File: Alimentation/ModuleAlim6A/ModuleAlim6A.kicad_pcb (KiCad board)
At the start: 4 copper layers, 66.5 x 39.8 mm, 19 parts, among them J1 Conn_01x05, J2 Conn_01x02, J3 OUTPUT, U1 PTN78020W_EUK-7, U2 ACS712xLCTR-20A

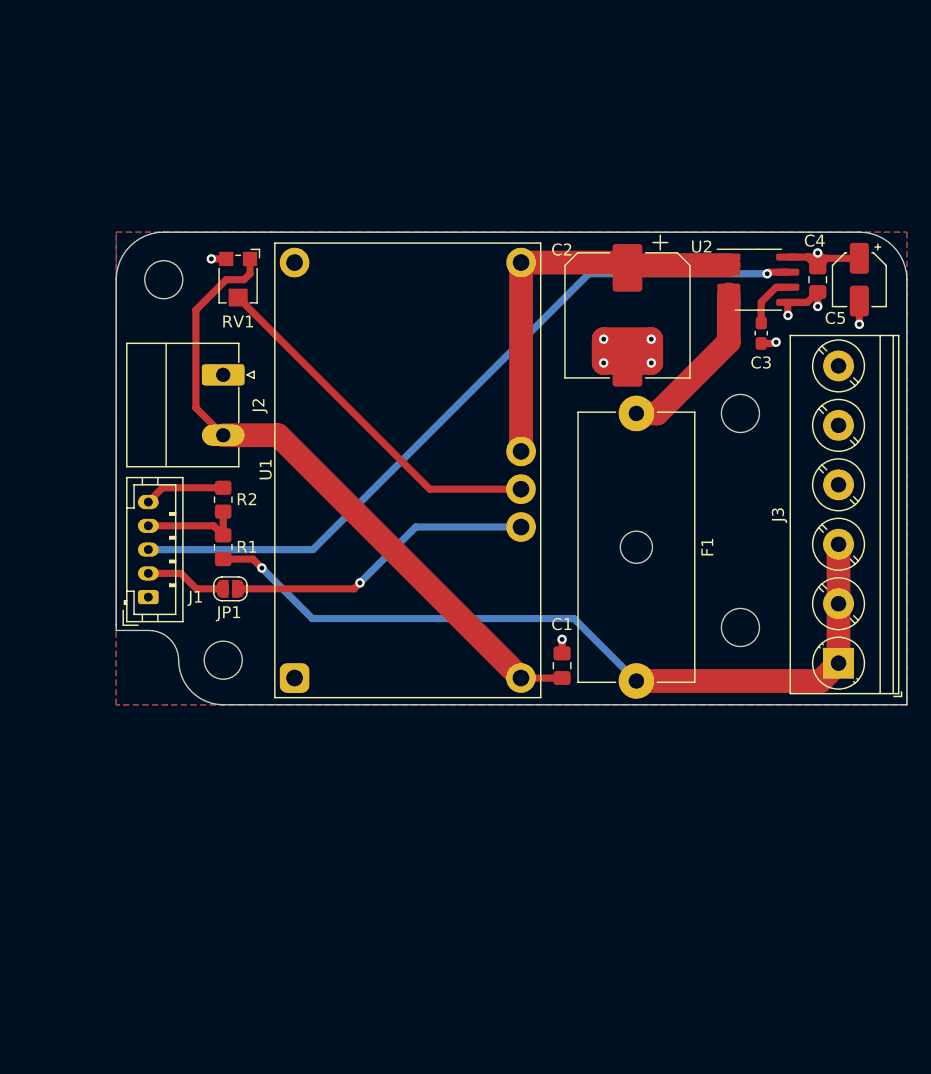
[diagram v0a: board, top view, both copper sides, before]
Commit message: Module alim ISO, clean master alim
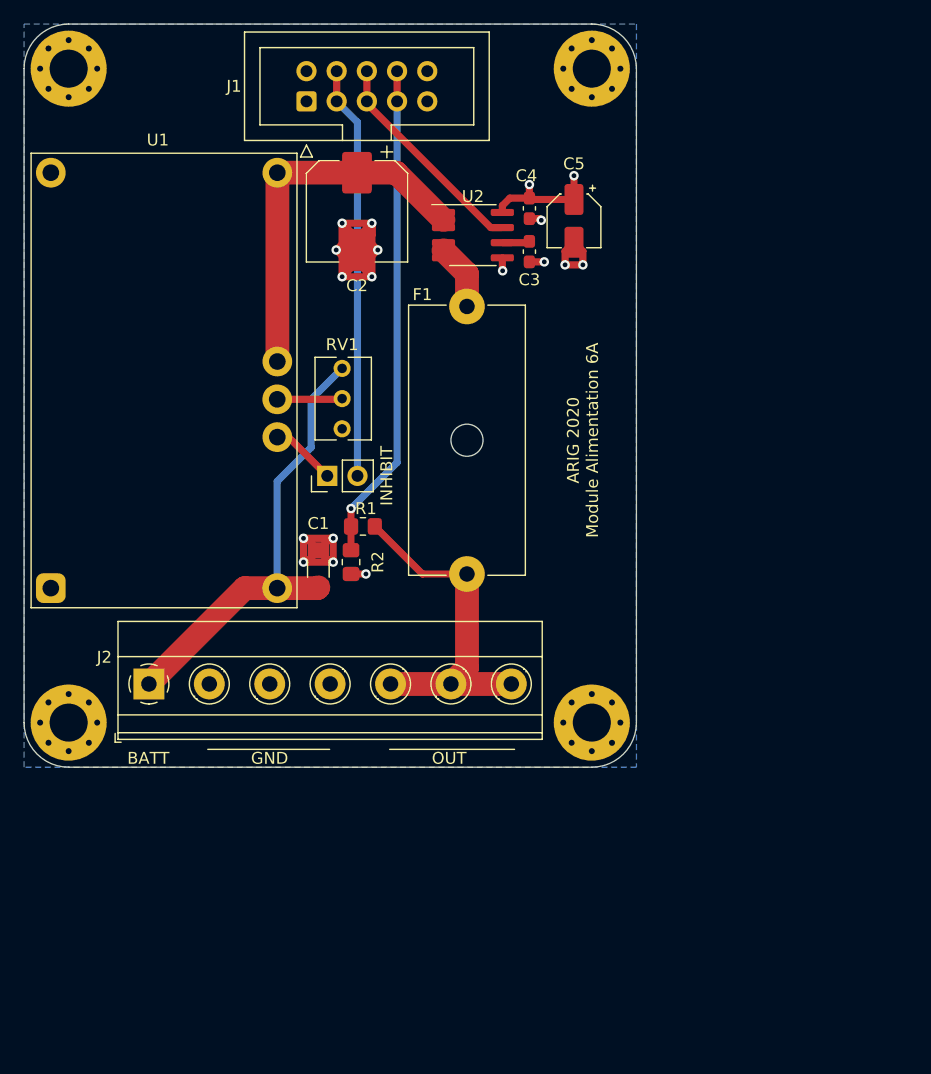
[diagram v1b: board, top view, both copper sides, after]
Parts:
- removed J3: OUTPUT, TerminalBlock_Phoenix:TerminalBlock_Phoenix_PT-1,5-6-5.0-H_1x06_P5.00mm_Horizontal
- removed JP1: /INHIBIT, Jumper:SolderJumper-2_P1.3mm_Open_RoundedPad1.0x1.5mm
- added J4: INHIBIT, Connector_PinHeader_2.54mm:PinHeader_1x02_P2.54mm_Vertical, F.Cu at (142.2, 85.5)
- C1: footprint Capacitor_SMD:C_0805_2012Metric_Pad1.18x1.45mm_HandSolder -> Capacitor_SMD:C_1206_3216Metric_Pad1.33x1.80mm_HandSolder
- C2: footprint Capacitor_SMD:CP_Elec_10x10 -> Capacitor_SMD:CP_Elec_8x10
- C4: footprint Capacitor_SMD:C_0805_2012Metric_Pad1.18x1.45mm_HandSolder -> Capacitor_SMD:C_0603_1608Metric_Pad1.08x0.95mm_HandSolder
- H1, H2, H3, H4: value MountingHole -> MountingHole_Pad; footprint MountingHole:MountingHole_3.2mm_M3 -> MountingHole:MountingHole_3.2mm_M3_Pad_Via
- J1: value Conn_01x05 -> Cmd; footprint Connector_JST:JST_PH_B5B-PH-K_1x05_P2.00mm_Vertical -> Connector_IDC:IDC-Header_2x05_P2.54mm_Vertical
- J2: value Conn_01x02 -> POWER; footprint Connector_Phoenix_MC_HighVoltage:PhoenixContact_MC_1,5_2-G-5.08_1x02_P5.08mm_Horizontal -> TerminalBlock_Phoenix:TerminalBlock_Phoenix_MKDS-1,5-7-5.08_1x07_P5.08mm_Horizontal
- RV1: footprint Potentiometer_SMD:Potentiometer_Bourns_TC33X_Vertical -> Potentiometer_THT:Potentiometer_Bourns_3266Y_Vertical
- moved H2 62.2 mm to (120.5, 106.2)
- moved H1 48.6 mm to (164.5, 51.2)
- moved J1 43.8 mm to (140.5, 54.0)
- moved H4 31.4 mm to (164.5, 106.2)
- moved J2 26.7 mm to (127.2, 103.0), turned to 0 degrees
- moved C4 25.0 mm to (159.2, 63.0)
- moved C5 24.5 mm to (163.0, 64.0)
- moved C2 24.4 mm to (144.8, 63.2)
- moved U2 24.3 mm to (154.5, 65.2)
- moved C1 22.1 mm to (141.5, 93.3)
- moved U1 21.8 mm to (119.0, 94.9)
- moved C3 20.7 mm to (159.2, 66.6)
- moved H3 19.5 mm to (120.5, 51.2)
- moved F1 16.9 mm to (154.0, 71.2)
- moved R2 12.0 mm to (144.2, 92.8), turned to 270 degrees
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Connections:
- H1 pad 1: (no net) -> GND
- H2 pad 1: (no net) -> GND
- H3 pad 1: (no net) -> GND
- H4 pad 1: (no net) -> GND
- J1 pad 2: /EN -> +5V
- J1 pad 3: /ANA_CURRENT -> /EN
- J1 pad 4: /ANA_VOLT -> /EN
- J1 pad 5: GND -> /ANA_CURRENT
- J2 pad 1: GND -> +BATT
- J2 pad 2: +BATT -> GND
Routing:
- net /ANA_CURRENT: track 63.4 -> 18.4 mm, vias 1 -> 0
- net /OUT: track 66.6 -> 29.4 mm, vias 1 -> 0
- net /ANA_VOLT: track 8.63 -> 41.9 mm, vias 0 -> 1
- net /EN: track 6.79 -> 34.8 mm
- net GND: track 29.7 -> 56.4 mm, vias 10 -> 16
- net Net-(RV1-Pad2): track 30.5 -> 5.48 mm
- net Net-(J4-Pad1): track 26.0 -> 5.55 mm, vias 1 -> 0
- net +BATT: track 55.5 -> 38.4 mm
- net Net-(F1-Pad1): track 15.5 -> 6.81 mm
- net Net-(C3-Pad1): track 4.50 -> 2.32 mm
- net /VO: track 34.9 -> 32.8 mm
- net +5V: vias 1 -> 2
- removed copper zone on F.Cu, net GND
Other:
- board size 66.5 x 39.8 mm -> 51.5 x 62.5 mm
- board text added: "ARIG 2020 Module Alimentation 6A"
- board text added: "BATT"
- board text added: "GND"
- board text added: "OUT"

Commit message: Modules Alim 3A et 6A uniforme sans mesure courant/tension
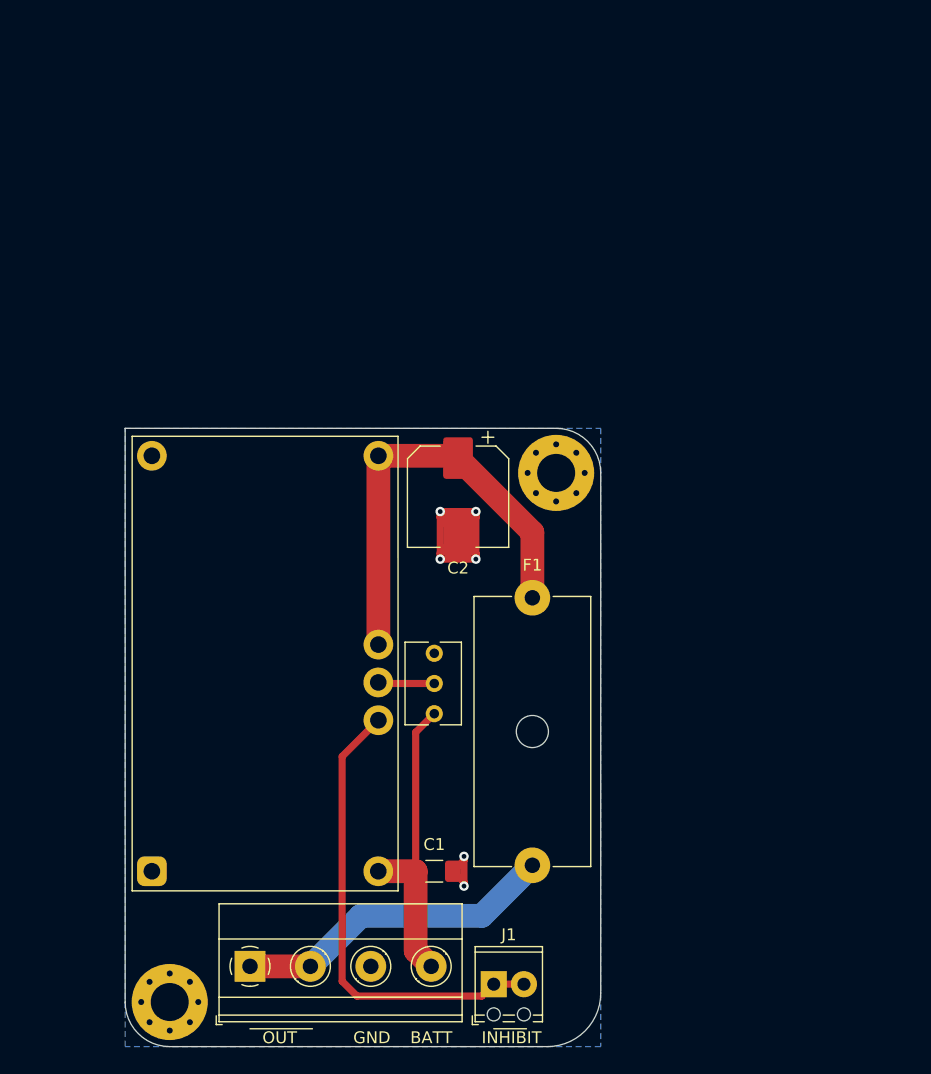
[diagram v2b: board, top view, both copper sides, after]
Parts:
- removed C3: 1n, Capacitor_SMD:C_0603_1608Metric_Pad1.08x0.95mm_HandSolder
- removed C4: 100n, Capacitor_SMD:C_0603_1608Metric_Pad1.08x0.95mm_HandSolder
- removed C5: 1u, Capacitor_SMD:CP_Elec_4x5.3
- removed H3, H4: MountingHole_Pad, MountingHole:MountingHole_3.2mm_M3_Pad_Via
- removed J4: INHIBIT, Connector_PinHeader_2.54mm:PinHeader_1x02_P2.54mm_Vertical
- removed R1: 10K, Resistor_SMD:R_0805_2012Metric_Pad1.20x1.40mm_HandSolder
- removed R2: 6.2K, Resistor_SMD:R_0805_2012Metric_Pad1.20x1.40mm_HandSolder
- removed U2: ACS712xLCTR-20A, Package_SO:SOIC-8_3.9x4.9mm_P1.27mm
- J1: value Cmd -> Inhibit; footprint Connector_IDC:IDC-Header_2x05_P2.54mm_Vertical -> TerminalBlock_Phoenix:TerminalBlock_Phoenix_MPT-0,5-2-2.54_1x02_P2.54mm_Horizontal
- J2: value POWER -> Alim. IN / OUT; footprint TerminalBlock_Phoenix:TerminalBlock_Phoenix_MKDS-1,5-7-5.08_1x07_P5.08mm_Horizontal -> TerminalBlock_Phoenix:TerminalBlock_Phoenix_MKDS-1,5-4-5.08_1x04_P5.08mm_Horizontal
- moved H1 86.2 mm to (129.0, 129.8)
- moved J1 75.9 mm to (156.2, 128.2), turned to 0 degrees
- moved F1 47.3 mm to (159.5, 118.2), turned to 90 degrees
- moved H2 46.1 mm to (161.5, 85.2)
- moved RV1 30.1 mm to (151.2, 105.5), turned to 270 degrees
- moved C1 27.2 mm to (151.2, 118.8), turned to 0 degrees
- moved C2 25.5 mm to (153.2, 87.2)
- moved U1 25.3 mm to (127.5, 118.8)
- moved J2 25.2 mm to (135.8, 126.8)
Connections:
- C2 pad 1: /VO -> Net-(C2-Pad1)
- F1 pad 1: Net-(F1-Pad1) -> /OUT
- F1 pad 2: /OUT -> Net-(C2-Pad1)
- J1 pad 1: +5V -> /EN
- J1 pad 2: +5V -> /EN
- J2 pad 1: +BATT -> /OUT
- J2 pad 2: GND -> /OUT
- J2 pad 4: GND -> +BATT
- U1 pad 3: Net-(J4-Pad1) -> /EN
- U1 pad 5: /VO -> Net-(C2-Pad1)
- U1 pad 6: /VO -> Net-(C2-Pad1)
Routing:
- net /ANA_VOLT: track 41.9 -> 0.00 mm, vias 1 -> 0
- net Net-(C2-Pad1): track 0.00 -> 37.0 mm
- net /VO: track 32.8 -> 0.00 mm
- net GND: track 56.4 -> 30.3 mm, vias 16 -> 6
- net /ANA_CURRENT: track 18.4 -> 0.00 mm
- net +BATT: track 38.4 -> 25.6 mm
- net +5V: track 10.0 -> 0.00 mm, vias 2 -> 0
- net Net-(F1-Pad1): track 6.81 -> 0.00 mm
- net Net-(J4-Pad1): track 5.55 -> 0.00 mm
- net /EN: track 34.8 -> 39.4 mm
- net Net-(C3-Pad1): track 2.32 -> 0.00 mm
- net /OUT: track 29.4 -> 27.3 mm
- net Net-(RV1-Pad2): track 5.48 -> 4.75 mm
- removed copper zone on In2.Cu, net +5V
- removed copper zone on In1.Cu, net GND
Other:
- board size 51.5 x 62.5 mm -> 40 x 52 mm
- copper layers 4 -> 2
- board text added: "INHIBIT"
- board text removed: "ARIG 2020 Module Alimentation 6A"

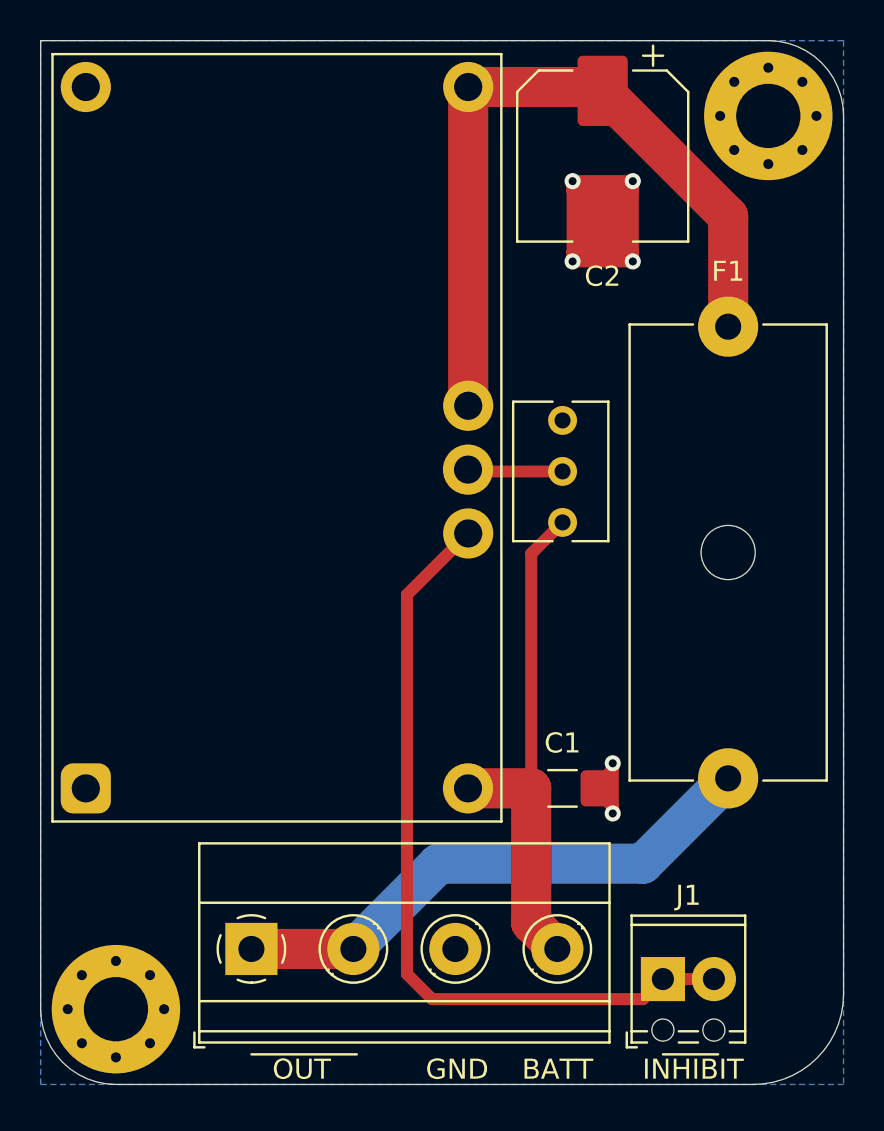
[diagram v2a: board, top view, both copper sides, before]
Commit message: Finalisation modules 3A et 6A, routage master alim
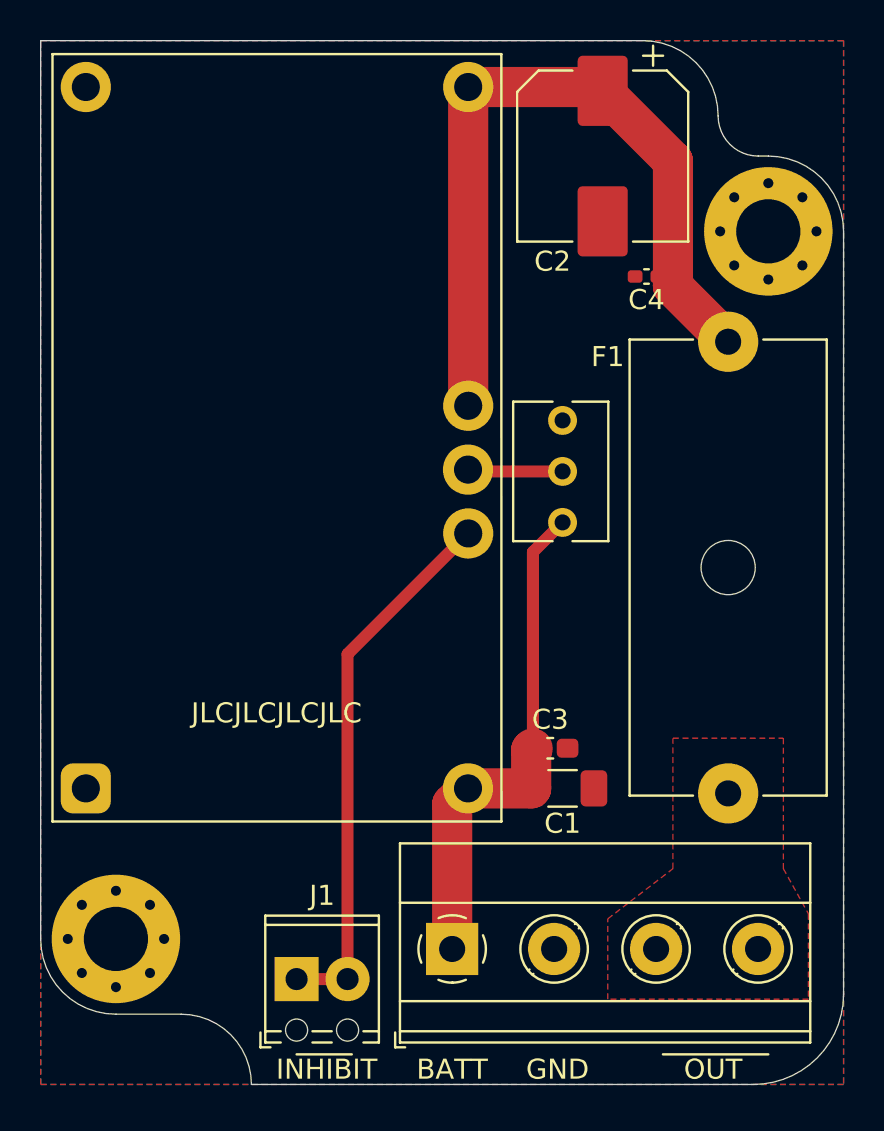
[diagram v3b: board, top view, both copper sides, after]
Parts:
- added C3: 1u, Capacitor_SMD:C_0603_1608Metric_Pad1.08x0.95mm_HandSolder, F.Cu at (150.6, 116.8)
- added C4: 1u, Capacitor_SMD:C_0402_1005Metric_Pad0.74x0.62mm_HandSolder, F.Cu at (155.4, 93.2)
- added G***: LOGO, ARIG:Logo_ARIG_12_6x6_6, B.Cu at (136.0, 100.0)
- moved J1 18.2 mm to (138.0, 128.2)
- moved J2 10.0 mm to (145.8, 126.8)
- moved H2 5.75 mm to (161.5, 91.0)
- moved H1 3.50 mm to (129.0, 126.2)
- moved F1 0.75 mm to (159.5, 119.0)
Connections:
- J2 pad 1: /OUT -> +BATT
- J2 pad 2: /OUT -> GND
- J2 pad 3: GND -> /OUT
- J2 pad 4: +BATT -> /OUT
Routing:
- net GND: track 30.3 -> 0.00 mm, vias 6 -> 0
- net /OUT: track 27.3 -> 0.00 mm
- net /EN: track 39.4 -> 27.3 mm
- net Net-(C2-Pad1): track 37.0 -> 37.7 mm
- added copper zone on F.Cu, net /OUT
- added copper zone on F.Cu, net GND
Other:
- outline, holes or cut-outs redrawn
- board text added: "Alimentation Module 6A 2020"
- board text added: "JLCJLCJLCJLC"

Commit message: Rework suite point robot
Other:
- outline, holes or cut-outs redrawn

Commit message: Finalisation alimentations
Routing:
- net /OUT: track 0.00 -> 22.7 mm
- net Net-(C2-Pad1): track 37.7 -> 52.3 mm
- net GND: track 0.00 -> 3.42 mm
- removed copper zone on F.Cu, net /OUT
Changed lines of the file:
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@@
     (thickness 1.6)
     (drawings 26)
-    (tracks 19)
+    (tracks 31)
     (zones 0)
     (modules 12)
@@
   )
   (setup
-    (last_trace_width 0.25)
+    (last_trace_width 4)
     (user_trace_width 0.6)
     (user_trace_width 2)
+    (user_trace_width 4)
     (trace_clearance 0.2)
     (zone_clearance 0.508)
@@
   (gr_line (start 165.25 91) (end 165.25 129) (layer Edge.Cuts) (width 0.05))
   (gr_line (start 125.25 81.5) (end 155.25 81.5) (layer Edge.Cuts) (width 0.05))
-  (segment (start 145.75 119.54) (end 146.54 118.75) (width 2) (layer F.Cu) (net 2))
-  (segment (start 145.75 126.75) (end 145.75 119.54) (width 2) (layer F.Cu) (net 2))
-  (segment (start 146.54 118.75) (end 149.6875 118.75) (width 2) (layer F.Cu) (net 2))
-  (segment (start 149.6875 116.8375) (end 149.76249 116.76251) (width 2) (layer F.Cu) (net 2))
-  (segment (start 149.6875 118.75) (end 149.6875 116.8375) (width 2) (layer F.Cu) (net 2))
+  (segment (start 154.865 92.115) (end 153.25 90.5) (width 0.6) (layer F.Cu) (net 1))
+  (segment (start 154.865 93.25) (end 154.865 92.115) (width 0.6) (layer F.Cu) (net 1))
   (segment (start 149.775 106.975) (end 151.25 105.5) (width 0.6) (layer F.Cu) (net 2))
   (segment (start 149.775 116.75) (end 149.775 106.975) (width 0.6) (layer F.Cu) (net 2))
+  (segment (start 145.75 119.54) (end 146.54 118.75) (width 4) (layer F.Cu) (net 2))
+  (segment (start 145.75 126.75) (end 145.75 119.54) (width 4) (layer F.Cu) (net 2))
+  (segment (start 146.54 118.75) (end 149.6875 118.75) (width 2) (layer F.Cu) (net 2))
+  (segment (start 149.6875 116.8375) (end 149.775 116.75) (width 0.6) (layer F.Cu) (net 2))
+  (segment (start 149.6875 118.75) (end 149.6875 116.8375) (width 0.6) (layer F.Cu) (net 2))
+  (segment (start 159.5 125.26) (end 160.99 126.75) (width 4) (layer F.Cu) (net 3))
+  (segment (start 159.5 119) (end 159.5 125.26) (width 4) (layer F.Cu) (net 3))
+  (segment (start 159.5 123.16) (end 155.91 126.75) (width 4) (layer F.Cu) (net 3))
+  (segment (start 159.5 119) (end 159.5 123.16) (width 4) (layer F.Cu) (net 3))
+  (segment (start 155.91 126.75) (end 160.99 126.75) (width 4) (layer F.Cu) (net 3))
   (segment (start 138 128.25) (end 140.54 128.25) (width 0.6) (layer F.Cu) (net 4))
   (segment (start 140.5 128.21) (end 140.54 128.25) (width 0.6) (layer F.Cu) (net 4))
@@
   (segment (start 146.63 102.96) (end 146.54 102.87) (width 0.6) (layer F.Cu) (net 5))
   (segment (start 151.25 102.96) (end 146.63 102.96) (width 0.6) (layer F.Cu) (net 5))
-  (segment (start 146.55 99.69) (end 146.55 83.81) (width 2) (layer F.Cu) (net 6))
-  (segment (start 153.06 83.81) (end 153.25 84) (width 2) (layer F.Cu) (net 6))
-  (segment (start 146.55 83.81) (end 153.06 83.81) (width 2) (layer F.Cu) (net 6))
-  (segment (start 159.5 96.5) (end 156.75 93.75) (width 2) (layer F.Cu) (net 6))
-  (segment (start 156.75 87.5) (end 153.25 84) (width 2) (layer F.Cu) (net 6))
-  (segment (start 156.75 93.75) (end 156.75 87.5) (width 2) (layer F.Cu) (net 6))
+  (segment (start 146.55 99.69) (end 146.55 83.81) (width 0.6) (layer F.Cu) (net 6))
+  (segment (start 153.06 83.81) (end 153.25 84) (width 4) (layer F.Cu) (net 6))
+  (segment (start 146.55 83.81) (end 153.06 83.81) (width 4) (layer F.Cu) (net 6))
+  (segment (start 159.25 96.5) (end 157.281495 94.531495) (width 4) (layer F.Cu) (net 6))
+  (segment (start 159.5 96.5) (end 159.25 96.5) (width 4) (layer F.Cu) (net 6))
+  (segment (start 153.28516 96.5) (end 159.5 96.5) (width 4) (layer F.Cu) (net 6))
+  (segment (start 149.79999 93.01483) (end 153.28516 96.5) (width 4) (layer F.Cu) (net 6))
+  (segment (start 149.79999 87.45001) (end 149.79999 93.01483) (width 4) (layer F.Cu) (net 6))
+  (segment (start 153.25 84) (end 149.79999 87.45001) (width 4) (layer F.Cu) (net 6))
+  (segment (start 149.79999 87.05999) (end 149.79999 87.45001) (width 4) (layer F.Cu) (net 6))
+  (segment (start 146.55 83.81) (end 149.79999 87.05999) (width 4) (layer F.Cu) (net 6))
   (zone (net 1) (net_name GND) (layer B.Cu) (hatch edge 0.508)
     (connect_pads (clearance 0.508))
@@
       )
     )
-  )
-  (zone (net 3) (net_name /OUT) (layer F.Cu) (hatch edge 0.508)
-    (priority 1)
-    (connect_pads (clearance 0.508))
-    (min_thickness 0.508)
-    (fill yes (arc_segments 32) (thermal_gap 0.508) (thermal_bridge_width 1.016) (smoothing fillet) (radius 2))
-    (polygon
-      (pts
-        (xy 162.25 122.75) (xy 163.5 125) (xy 163.5 129.25) (xy 153.5 129.25) (xy 153.5 125.25)
-        (xy 156.75 122.75) (xy 156.75 116.25) (xy 162.25 116.25)
-      )
-    )

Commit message: Finalisation pour commande pack Alimentation 14/02/2021
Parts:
- C3: footprint Capacitor_SMD:C_0603_1608Metric_Pad1.08x0.95mm_HandSolder -> Capacitor_SMD:C_0805_2012Metric_Pad1.18x1.45mm_HandSolder
- moved C3 0.51 mm to (150.8, 116.2)
